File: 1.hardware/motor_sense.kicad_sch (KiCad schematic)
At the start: 52 parts, among them IC7 SN74HCS266QDRQ1, IC8 SN74HC74PWRG4, IC9 SN74LVC3G17DCURG4, U10 TLV9064, U9 TLV9064

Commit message: 풋프린트 연결 완료
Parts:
- IC7: footprint SamacSys_Parts:SOIC127P600X175-14N -> SamacSys_Parts_Project:SOIC127P600X175-14N
- IC8: footprint SamacSys_Parts:SOP65P640X120-14N -> SamacSys_Parts_Project:SOP65P640X120-14N
- IC9: footprint SamacSys_Parts:SOP50P310X90-8N -> SamacSys_Parts_Project:SOP50P310X90-8N
- U10, U9: footprint (none) -> Package_SO:TSSOP-14_4.4x5mm_P0.65mm
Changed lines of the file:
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@@
 			)
 		)
-		(property "Footprint" ""
+		(property "Footprint" "Package_SO:TSSOP-14_4.4x5mm_P0.65mm"
 			(at 191.77 149.86 0)
 			(effects
@@
 			)
 		)
-		(property "Footprint" ""
+		(property "Footprint" "Package_SO:TSSOP-14_4.4x5mm_P0.65mm"
 			(at 191.77 29.21 0)
 			(effects
@@
 			)
 		)
-		(property "Footprint" ""
+		(property "Footprint" "Package_SO:TSSOP-14_4.4x5mm_P0.65mm"
 			(at 275.59 173.99 0)
 			(effects
@@
 			)
 		)
-		(property "Footprint" "SamacSys_Parts:SOIC127P600X175-14N"
+		(property "Footprint" "SamacSys_Parts_Project:SOIC127P600X175-14N"
 			(at 58.42 44.45 0)
 			(effects
@@
 			)
 		)
-		(property "Footprint" ""
+		(property "Footprint" "Package_SO:TSSOP-14_4.4x5mm_P0.65mm"
 			(at 275.59 157.48 0)
 			(effects
@@
 			)
 		)
-		(property "Footprint" "SamacSys_Parts:SOP65P640X120-14N"
+		(property "Footprint" "SamacSys_Parts_Project:SOP65P640X120-14N"
 			(at 83.82 157.48 0)
 			(effects
@@
 			)
 		)
-		(property "Footprint" ""
+		(property "Footprint" "Package_SO:TSSOP-14_4.4x5mm_P0.65mm"
 			(at 207.01 170.18 0)
 			(effects
@@
 			)
 		)
-		(property "Footprint" "SamacSys_Parts:SOP50P310X90-8N"
+		(property "Footprint" "SamacSys_Parts_Project:SOP50P310X90-8N"
 			(at 80.01 95.25 0)
 			(effects
@@
 			)
 		)
-		(property "Footprint" ""
+		(property "Footprint" "Package_SO:TSSOP-14_4.4x5mm_P0.65mm"
 			(at 229.87 59.69 0)
 			(effects
@@
 			)
 		)
-		(property "Footprint" ""
+		(property "Footprint" "Package_SO:TSSOP-14_4.4x5mm_P0.65mm"
 			(at 275.59 139.7 0)
 			(effects
@@
 			)
 		)
-		(property "Footprint" ""
+		(property "Footprint" "Package_SO:TSSOP-14_4.4x5mm_P0.65mm"
 			(at 212.09 39.37 0)
 			(effects
@@
 			)
 		)
-		(property "Footprint" ""
+		(property "Footprint" "Package_SO:TSSOP-14_4.4x5mm_P0.65mm"
 			(at 229.87 104.14 0)
 			(effects
@@
 			)
 		)
-		(property "Footprint" ""
+		(property "Footprint" "Package_SO:TSSOP-14_4.4x5mm_P0.65mm"
 			(at 229.87 81.28 0)
 			(effects

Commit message: 중간 저장
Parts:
- added C125: 0.1uF/50V, Capacitor_SMD:C_0603_1608Metric, symbol Device:C_Small_US
- added IC9: SN74LVC3G17DCURG4, SamacSys_Parts_Project:SOP50P310X90-8N, symbol SamacSys_Parts:SN74LVC3G17DCURG4
- renumbered IC7 to IC6, IC8 to IC7, IC9 to IC8, R171 to R156, R172 to R157, R173 to R158, R174 to R159, R175 to R160, R176 to R161, R177 to R162, R178 to R163, R179 to R164, R180 to R165, R181 to R166, R182 to R167, R183 to R168, R184 to R169, R185 to R170, R186 to R171, R187 to R172, R188 to R173, R189 to R174, R190 to R175, R191 to R176, R192 to R177, R193 to R178, R194 to R179, R195 to R180, R196 to R181, TP18 to TP16, TP19 to TP17, TP20 to TP18, TP21 to TP19, TP22 to TP20, TP23 to TP21, TP24 to TP22, TP25 to TP23
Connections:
- net 3V3_MCU: now also C125.1, IC9.8 (VCC)
- net GND: now also C125.2, IC9.4 (GND)
- net MOTOR_U_SHUNT_ADC: now also IC9.1 (1A)
- net MOTOR_V_SHUNT_ADC: now also IC9.2 (3Y)
- net MOTOR_W_SHUNT_ADC: now also IC9.3 (2A)
- new net MOTOR_U_SHUNT_SCH: IC9.7 (1Y)
- new net MOTOR_V_SHUNT_SCH: IC9.6 (3A)
- new net MOTOR_W_SHUNT_SCH: IC9.5 (2Y)

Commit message: 중간 저장
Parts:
- renumbered C117 to C107, C114 to C108, C122 to C109, C123 to C110, C125 to C111, C113 to C112, C115 to C113, C124 to C114, C119 to C115, C118 to C116, C120 to C117, C112 to C118, C116 to C119, C121 to C120, IC7 to IC10, IC6 to IC7, IC9 to IC8, IC8 to IC9, R156 to R146, R158 to R147, R160 to R148, R161 to R149, R176 to R150, R162 to R151, R170 to R152, R163 to R153, R177 to R154, R164 to R155, R171 to R156, R159 to R157, R165 to R158, R178 to R159, R166 to R160, R172 to R161, R167 to R162, R179 to R163, R173 to R164, R157 to R165, R168 to R166, R180 to R167, R174 to R168, R181 to R170, R175 to R171, TP18 to TP15, TP19 to TP16, TP16 to TP17, TP20 to TP18, TP21 to TP19, TP22 to TP20, TP17 to TP21, TP23 to TP22, U9 to U23, U10 to U24
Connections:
- net MOTOR_V_SHUNT_M is gone; now on net GNDPWR: R155.1
- net MOTOR_W_SHUNT_M is gone; now on net GNDPWR: R160.1
- net MOTOR_U_SHUNT_M renamed GNDPWR

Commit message: 오류 일단 다 잡음
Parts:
- C107, C108, C111, C112, C113, C115, C116, C117, C119, C120: footprint Capacitor_SMD:C_0603_1608Metric -> Capacitor_SMD:C_0402_1005Metric
- R150, R154, R159: footprint Resistor_SMD:R_0402_1005Metric -> Resistor_SMD:R_0603_1608Metric
- R152, R156, R161: footprint Resistor_SMD:R_0402_1005Metric -> Resistor_SMD:R_0805_2012Metric
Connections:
- net ADC_VREF_2V5 is gone; now on net 3V3: C107.1, U23.4 (V+)
- net 3V3_MCU renamed 3V3
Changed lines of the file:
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@@
 	(wire
 		(pts
-			(xy 81.28 46.99) (xy 81.28 49.53)
-		)
-		(stroke
-			(width 0)
-			(type default)
-		)
-	)
-	(wire
-		(pts
 			(xy 254 175.26) (xy 254 172.72)
 		)
@@
 	(wire
 		(pts
+			(xy 81.28 48.26) (xy 81.28 49.53)
+		)
+		(stroke
+			(width 0)
+			(type default)
+		)
+	)
+	(wire
+		(pts
 			(xy 204.47 59.69) (xy 209.55 59.69)
 		)
@@
 	(wire
 		(pts
+			(xy 87.63 48.26) (xy 81.28 48.26)
+		)
+		(stroke
+			(width 0)
+			(type default)
+		)
+	)
+	(wire
+		(pts
 			(xy 31.75 157.48) (xy 31.75 160.02)
 		)
@@
 		)
 	)
-	(global_label "ADC_VREF_2V5"
+	(global_label "MOTOR_W_SHUNT_ADC"
 		(shape passive)
-		(at 205.74 21.59 0)
+		(at 311.15 87.63 180)
 		(fields_autoplaced yes)
 		(effects
@@
 				(size 1.27 1.27)
 			)
-			(justify left)
+			(justify right)
 		)
 		(property "Intersheetrefs" "${INTERSHEET_REFS}"
-			(at 221.2815 21.59 0)
+			(at 288.7747 87.63 0)
 			(effects
 				(font
 					(size 1.27 1.27)
 				)
-				(justify left)
+				(justify right)
 				(hide yes)
 			)
 		)
 	)
-	(global_label "MOTOR_W_SHUNT_ADC"
+	(global_label "3V3"
 		(shape passive)
-		(at 311.15 87.63 180)
+		(at 205.74 21.59 0)
 		(fields_autoplaced yes)
 		(effects
@@
 				(size 1.27 1.27)
 			)
-			(justify right)
+			(justify left)
 		)
 		(property "Intersheetrefs" "${INTERSHEET_REFS}"
-			(at 288.7747 87.63 0)
+			(at 211.1215 21.59 0)
 			(effects
 				(font
 					(size 1.27 1.27)
 				)
-				(justify right)
+				(justify left)
 				(hide yes)
 			)
@@
 		)
 	)
-	(global_label "3V3_MCU"
+	(global_label "3V3"
 		(shape passive)
-		(at 351.79 82.55 0)
+		(at 87.63 48.26 0)
 		(fields_autoplaced yes)
 		(effects
@@
 		)
 		(property "Intersheetrefs" "${INTERSHEET_REFS}"
-			(at 362.191 82.55 0)
+			(at 93.0115 48.26 0)
 			(effects
 				(font
@@
 		)
 	)
+	(global_label "3V3"
+		(shape passive)
+		(at 351.79 82.55 0)
+		(fields_autoplaced yes)
+		(effects
+			(font
+				(size 1.27 1.27)
+			)
+			(justify left)
+		)
+		(property "Intersheetrefs" "${INTERSHEET_REFS}"
+			(at 357.1715 82.55 0)
+			(effects
+				(font
+					(size 1.27 1.27)
+				)
+				(justify left)
+				(hide yes)
+			)
+		)
+	)
 	(global_label "ZC_UV_1"
 		(shape passive)
@@
 		)
 	)
-	(global_label "3V3_MCU"
-		(shape passive)
-		(at 204.47 140.97 0)
-		(fields_autoplaced yes)
-		(effects
-			(font
-				(size 1.27 1.27)
-			)
-			(justify left)
-		)
-		(property "Intersheetrefs" "${INTERSHEET_REFS}"
-			(at 214.871 140.97 0)
-			(effects
-				(font
-					(size 1.27 1.27)
-				)
-				(justify left)
-				(hide yes)
-			)
-		)
-	)
 	(global_label "ZC_VW_3"
 		(shape passive)
@@
 		)
 	)
-	(global_label "3V3_MCU"
+	(global_label "HALL_A"
 		(shape passive)
-		(at 81.28 46.99 0)
+		(at 21.59 46.99 180)
 		(fields_autoplaced yes)
 		(effects
@@
 				(size 1.27 1.27)
 			)
-			(justify left)
+			(justify right)
 		)
 		(property "Intersheetrefs" "${INTERSHEET_REFS}"
-			(at 91.681 46.99 0)
+			(at 13.1846 46.99 0)
 			(effects
 				(font
 					(size 1.27 1.27)
 				)
-				(justify left)
+				(justify right)
 				(hide yes)
 			)
 		)
 	)
-	(global_label "HALL_A"
+	(global_label "MOTOR_W_SHUNT_P"
 		(shape passive)
-		(at 21.59 46.99 180)
+		(at 204.47 104.14 180)
 		(fields_autoplaced yes)
 		(effects
@@
 		)
 		(property "Intersheetrefs" "${INTERSHEET_REFS}"
-			(at 13.1846 46.99 0)
+			(at 184.4533 104.14 0)
 			(effects
 				(font
@@
 		)
 	)
-	(global_label "MOTOR_W_SHUNT_P"
+	(global_label "3V3"
 		(shape passive)
-		(at 204.47 104.14 180)
+		(at 204.47 140.97 0)
 		(fields_autoplaced yes)
 		(effects
@@
 				(size 1.27 1.27)
 			)
-			(justify right)
+			(justify left)
 		)
 		(property "Intersheetrefs" "${INTERSHEET_REFS}"
-			(at 184.4533 104.14 0)
+			(at 209.8515 140.97 0)
 			(effects
 				(font
 					(size 1.27 1.27)
 				)
-				(justify right)
+				(justify left)
 				(hide yes)
 			)
@@
 			)
 		)
-		(property "Footprint" "Resistor_SMD:R_0402_1005Metric"
+		(property "Footprint" "Resistor_SMD:R_0603_1608Metric"
 			(at 248.92 83.82 0)
 			(effects
@@
 			)
 		)
-		(property "Footprint" "Capacitor_SMD:C_0603_1608Metric"
+		(property "Footprint" "Capacitor_SMD:C_0402_1005Metric"
 			(at 44.45 105.41 0)
 			(effects
@@
 			)
 		)
-		(property "Footprint" "Capacitor_SMD:C_0603_1608Metric"
+		(property "Footprint" "Capacitor_SMD:C_0402_1005Metric"
 			(at 200.66 27.94 0)
 			(effects
@@
 			)
 		)
-		(property "Footprint" "Resistor_SMD:R_0402_1005Metric"
+		(property "Footprint" "Resistor_SMD:R_0603_1608Metric"
 			(at 250.19 106.68 0)
 			(effects
@@
 			)
 		)
-		(property "Footprint" "Capacitor_SMD:C_0603_1608Metric"
+		(property "Footprint" "Capacitor_SMD:C_0402_1005Metric"
 			(at 254 144.78 0)
 			(effects
@@
 			)
 		)
-		(property "Footprint" "Resistor_SMD:R_0402_1005Metric"
+		(property "Footprint" "Resistor_SMD:R_0603_1608Metric"
 			(at 248.92 62.23 0)
 			(effects
@@
 			)
 		)
-		(property "Footprint" "Resistor_SMD:R_0402_1005Metric"
+		(property "Footprint" "Resistor_SMD:R_0805_2012Metric"
 			(at 238.76 91.44 0)
 			(effects
@@
 			)
 		)
-		(property "Footprint" "Capacitor_SMD:C_0603_1608Metric"
+		(property "Footprint" "Capacitor_SMD:C_0402_1005Metric"
 			(at 92.71 166.37 0)
 			(effects
@@
 			)
 		)
-		(property "Footprint" "Capacitor_SMD:C_0603_1608Metric"
+		(property "Footprint" "Capacitor_SMD:C_0402_1005Metric"
 			(at 66.04 53.34 0)
 			(effects
@@
 			)
 		)
-		(property "Footprint" "Resistor_SMD:R_0402_1005Metric"
+		(property "Footprint" "Resistor_SMD:R_0805_2012Metric"
 			(at 238.76 114.3 0)
 			(effects
@@
 			)
 		)
-		(property "Footprint" "Capacitor_SMD:C_0603_1608Metric"
+		(property "Footprint" "Capacitor_SMD:C_0402_1005Metric"
 			(at 87.63 110.49 0)
 			(effects
@@
 			)
 		)
-		(property "Footprint" "Capacitor_SMD:C_0603_1608Metric"
+		(property "Footprint" "Capacitor_SMD:C_0402_1005Metric"
 			(at 254 177.8 0)
 			(effects
@@
 			)
 		)
-		(property "Footprint" "Resistor_SMD:R_0402_1005Metric"
+		(property "Footprint" "Resistor_SMD:R_0805_2012Metric"
 			(at 238.76 69.85 0)
 			(effects
@@
 			)
 		)
-		(property "Footprint" "Capacitor_SMD:C_0603_1608Metric"
+		(property "Footprint" "Capacitor_SMD:C_0402_1005Metric"
 			(at 346.71 95.25 0)
 			(effects
@@
 			)
 		)
-		(property "Footprint" "Capacitor_SMD:C_0603_1608Metric"
+		(property "Footprint" "Capacitor_SMD:C_0402_1005Metric"
 			(at 254 161.29 0)
 			(effects
@@
 			)
 		)
-		(property "Footprint" "Capacitor_SMD:C_0603_1608Metric"
+		(property "Footprint" "Capacitor_SMD:C_0402_1005Metric"
 			(at 200.66 147.32 0)
 			(effects

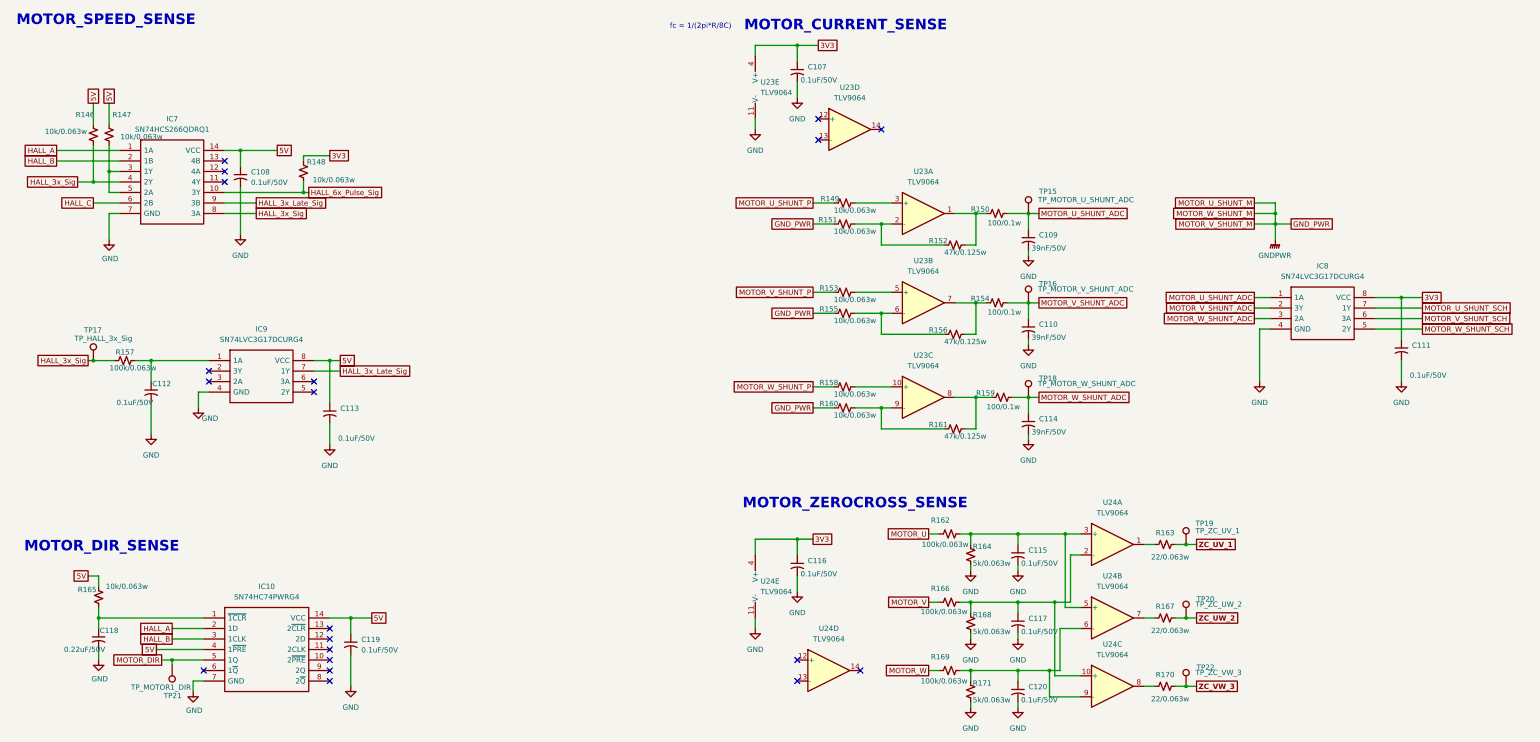
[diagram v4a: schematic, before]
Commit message: 부품 통일 및 필터 부분 캡 선정등 필요해보임
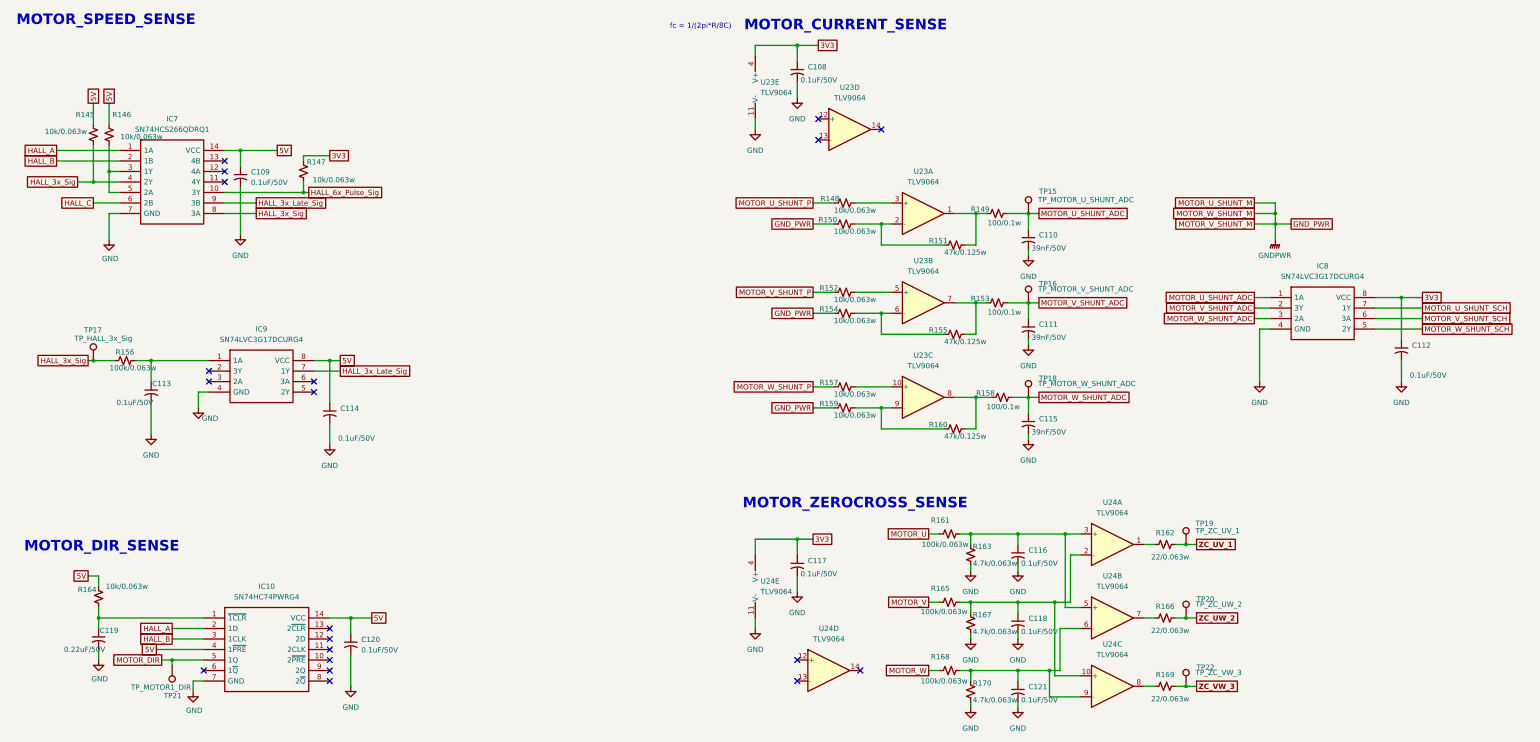
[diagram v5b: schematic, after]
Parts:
- R163: renamed from R164; value 5k/0.063w -> 4.7k/0.063w
- R167: renamed from R168; value 5k/0.063w -> 4.7k/0.063w
- R170: renamed from R171; value 5k/0.063w -> 4.7k/0.063w
- TP15, TP16, TP17, TP18, TP19, TP20, TP21, TP22: now left out of the parts list
- renumbered C107 to C108, C108 to C109, C109 to C110, C110 to C111, C111 to C112, C112 to C113, C113 to C114, C114 to C115, C115 to C116, C116 to C117, C117 to C118, C118 to C119, C119 to C120, C120 to C121, R146 to R145, R147 to R146, R148 to R147, R149 to R148, R150 to R149, R151 to R150, R152 to R151, R153 to R152, R154 to R153, R155 to R154, R156 to R155, R157 to R156, R158 to R157, R159 to R158, R160 to R159, R161 to R160, R162 to R161, R163 to R162, R165 to R164, R166 to R165, R167 to R166, R169 to R168, R170 to R169

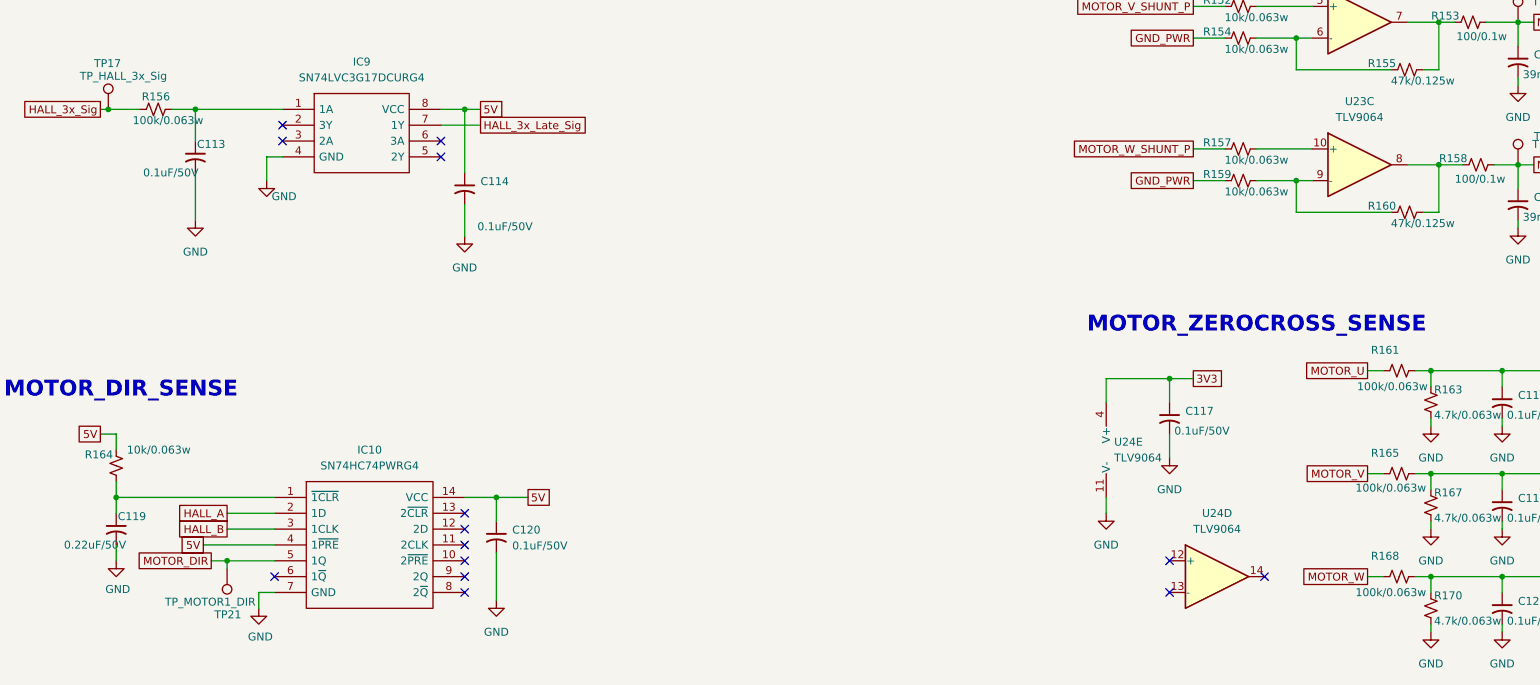
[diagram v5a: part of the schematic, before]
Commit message: 거의 완성 근데 JLC에서 포지션이 좀 개판임
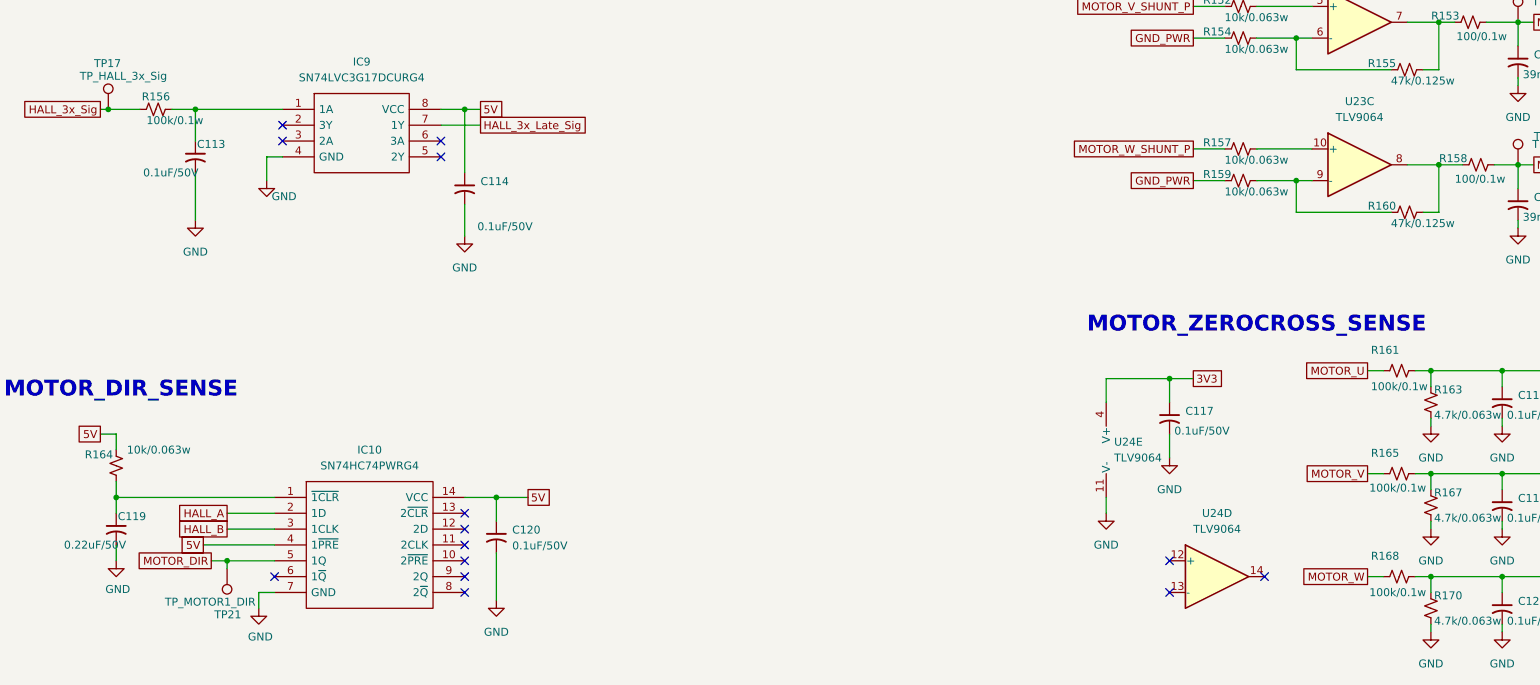
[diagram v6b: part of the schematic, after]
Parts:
- C110, C111, C115: footprint Capacitor_SMD:C_0402_1005Metric -> Capacitor_SMD:C_0603_1608Metric
- R156, R161, R165, R168: value 100k/0.063w -> 100k/0.1w; footprint Resistor_SMD:R_0402_1005Metric -> Resistor_SMD:R_0603_1608Metric
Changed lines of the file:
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@@
 			)
 		)
-		(property "Value" "100k/0.063w"
+		(property "Value" "100k/0.1w"
 			(at 45.72 99.568 90)
 			(effects
@@
 			)
 		)
-		(property "Footprint" "Resistor_SMD:R_0402_1005Metric"
+		(property "Footprint" "Resistor_SMD:R_0603_1608Metric"
 			(at 38.1 97.79 0)
 			(effects
@@
 			)
 		)
-		(property "Footprint" "Capacitor_SMD:C_0402_1005Metric"
+		(property "Footprint" "Capacitor_SMD:C_0603_1608Metric"
 			(at 256.54 68.58 0)
 			(effects
@@
 			)
 		)
-		(property "Footprint" "Capacitor_SMD:C_0402_1005Metric"
+		(property "Footprint" "Capacitor_SMD:C_0603_1608Metric"
 			(at 256.54 113.03 0)
 			(effects
@@
 			)
 		)
-		(property "Value" "100k/0.063w"
+		(property "Value" "100k/0.1w"
 			(at 241.808 158.496 90)
 			(effects
@@
 			)
 		)
-		(property "Footprint" "Resistor_SMD:R_0402_1005Metric"
+		(property "Footprint" "Resistor_SMD:R_0603_1608Metric"
 			(at 237.49 156.21 0)
 			(effects
@@
 			)
 		)
-		(property "Footprint" "Capacitor_SMD:C_0402_1005Metric"
+		(property "Footprint" "Capacitor_SMD:C_0603_1608Metric"
 			(at 256.54 90.17 0)
 			(effects
@@
 			)
 		)
-		(property "Value" "100k/0.063w"
+		(property "Value" "100k/0.1w"
 			(at 242.062 142.24 90)
 			(effects
@@
 			)
 		)
-		(property "Footprint" "Resistor_SMD:R_0402_1005Metric"
+		(property "Footprint" "Resistor_SMD:R_0603_1608Metric"
 			(at 237.49 139.7 0)
 			(effects
@@
 			)
 		)
-		(property "Value" "100k/0.063w"
+		(property "Value" "100k/0.1w"
 			(at 241.808 175.26 90)
 			(effects
@@
 			)
 		)
-		(property "Footprint" "Resistor_SMD:R_0402_1005Metric"
+		(property "Footprint" "Resistor_SMD:R_0603_1608Metric"
 			(at 237.49 172.72 0)
 			(effects
